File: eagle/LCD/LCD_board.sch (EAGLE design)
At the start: 7 parts, among them CN1 1X4-CLEANBIG

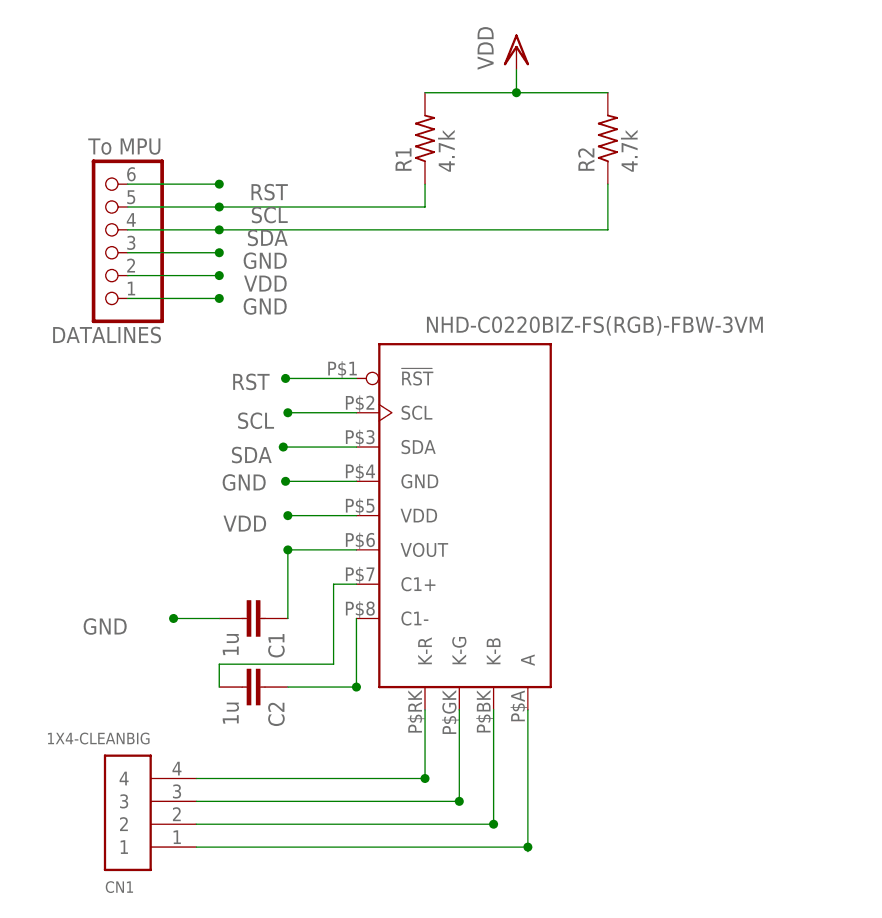
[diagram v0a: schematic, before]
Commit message: Updated LCD_board.sch with modified LCD screen schematic.
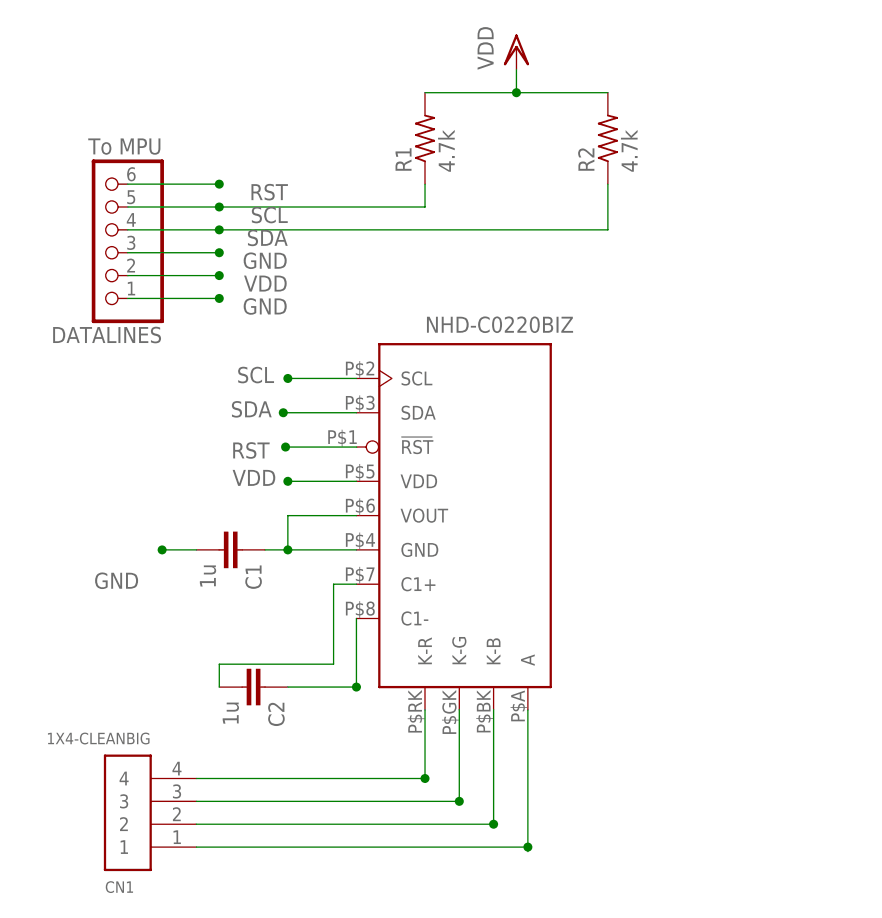
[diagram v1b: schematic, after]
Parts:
- U$1: value NHD-C0220BIZ-FS(RGB)-FBW-3VM -> NHD-C0220BIZ; device LockBox:NHD-C0220BIZ-FS(RGB)-FBW-3VM -> LockBox:NHD-C0220BIZ
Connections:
- net GND: no longer U$1.GND
- net N$3: now also U$1.GND
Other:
- moved on the sheet: C1
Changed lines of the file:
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@@
 <setting verticaltext="up"/>
 </settings>
-<grid distance="0.1" unitdist="inch" unit="inch" style="lines" multiple="1" display="no" altdistance="0.01" altunitdist="inch" altunit="inch"/>
+<grid distance="0.05" unitdist="inch" unit="inch" style="lines" multiple="1" display="yes" altdistance="0.01" altunitdist="inch" altunit="inch"/>
 <layers>
 <layer number="1" name="Top" color="4" fill="1" visible="no" active="no"/>
@@
 </classes>
 <parts>
-<part name="U$1" library="LockBox" deviceset="NHD-C0220BIZ-FS(RGB)-FBW-3VM" device=""/>
 <part name="DATALINES" library="adafruit" deviceset="PINHD-1X6" device="" value="To MPU">
 <attribute name="DATALINES" value=""/>
@@
 <part name="R2" library="LockBox" deviceset="R-US_" device="0204/5" value="4.7k"/>
 <part name="VDD1" library="supply1" deviceset="VDD" device=""/>
+<part name="U$1" library="LockBox" deviceset="NHD-C0220BIZ" device=""/>
 </parts>
 <sheets>
@@
 </plain>
 <instances>
-<instance part="U$1" gate="G$1" x="104.14" y="33.02"/>
 <instance part="DATALINES" gate="A" x="63.5" y="63.5" smashed="yes" rot="R180">
 <attribute name="NAME" x="69.85" y="52.705" size="1.778" layer="95" rot="R180"/>
@@
 <attribute name="DATALINES" x="63.5" y="63.5" size="1.778" layer="96" rot="R180" display="off"/>
 </instance>
-<instance part="C1" gate="G$1" x="81.28" y="20.32" rot="R270"/>
+<instance part="C1" gate="G$1" x="78.74" y="27.94" rot="R270"/>
 <instance part="C2" gate="G$1" x="81.28" y="12.7" rot="R270"/>
 <instance part="CN1" gate="G$1" x="68.58" y="-2.54" rot="R180"/>
@@
 <instance part="R2" gate="G$1" x="119.38" y="73.66" rot="R90"/>
 <instance part="VDD1" gate="G$1" x="109.22" y="83.82"/>
+<instance part="U$1" gate="G$1" x="104.14" y="33.02"/>
 </instances>
 <busses>
@@
 <net name="N$1" class="0">
 <segment>
-<pinref part="U$1" gate="G$1" pin="C1-"/>
 <pinref part="C2" gate="G$1" pin="1"/>
 <wire x1="91.44" y1="20.32" x2="91.44" y2="12.7" width="0.1524" layer="91"/>
 <wire x1="91.44" y1="12.7" x2="83.82" y2="12.7" width="0.1524" layer="91"/>
 <junction x="91.44" y="12.7"/>
+<pinref part="U$1" gate="G$1" pin="C1-"/>
 </segment>
 </net>
@@
 <wire x1="76.2" y1="15.24" x2="88.9" y2="15.24" width="0.1524" layer="91"/>
 <wire x1="88.9" y1="15.24" x2="88.9" y2="24.13" width="0.1524" layer="91"/>
+<wire x1="91.44" y1="24.13" x2="88.9" y2="24.13" width="0.1524" layer="91"/>
 <pinref part="U$1" gate="G$1" pin="C1+"/>
-<wire x1="91.44" y1="24.13" x2="88.9" y2="24.13" width="0.1524" layer="91"/>
 </segment>
 </net>
 <net name="N$3" class="0">
 <segment>
-<pinref part="U$1" gate="G$1" pin="VOUT"/>
 <wire x1="91.44" y1="27.94" x2="83.82" y2="27.94" width="0.1524" layer="91"/>
 <pinref part="C1" gate="G$1" pin="1"/>
-<wire x1="83.82" y1="27.94" x2="83.82" y2="20.32" width="0.1524" layer="91"/>
+<wire x1="83.82" y1="27.94" x2="81.28" y2="27.94" width="0.1524" layer="91"/>
 <junction x="83.82" y="27.94"/>
+<pinref part="U$1" gate="G$1" pin="GND"/>
+<pinref part="U$1" gate="G$1" pin="VOUT"/>
+<wire x1="91.44" y1="31.75" x2="83.82" y2="31.75" width="0.1524" layer="91"/>
+<wire x1="83.82" y1="31.75" x2="83.82" y2="27.94" width="0.1524" layer="91"/>
 </segment>
 </net>
 <net name="RST" class="0">
 <segment>
-<junction x="83.566" y="46.99"/>
-<label x="81.788" y="47.498" size="1.778" layer="95" rot="R180"/>
+<junction x="83.566" y="39.37"/>
+<label x="81.788" y="39.878" size="1.778" layer="95" rot="R180"/>
+<wire x1="91.44" y1="39.37" x2="83.566" y2="39.37" width="0.1524" layer="91"/>
 <pinref part="U$1" gate="G$1" pin="!RST"/>
-<wire x1="91.44" y1="46.99" x2="83.566" y2="46.99" width="0.1524" layer="91"/>
 </segment>
 <segment>
@@
 </segment>
 <segment>
+<wire x1="91.44" y1="46.99" x2="83.82" y2="46.99" width="0.1524" layer="91"/>
+<junction x="83.82" y="46.99"/>
+<label x="82.296" y="48.26" size="1.778" layer="95" rot="R180"/>
 <pinref part="U$1" gate="G$1" pin="SCL"/>
-<wire x1="91.44" y1="43.18" x2="83.82" y2="43.18" width="0.1524" layer="91"/>
-<junction x="83.82" y="43.18"/>
-<label x="82.296" y="43.18" size="1.778" layer="95" rot="R180"/>
 </segment>
 </net>
@@
 </segment>
 <segment>
+<wire x1="91.44" y1="43.18" x2="83.312" y2="43.18" width="0.1524" layer="91"/>
+<junction x="83.312" y="43.18"/>
+<label x="82.042" y="44.45" size="1.778" layer="95" rot="R180"/>
 <pinref part="U$1" gate="G$1" pin="SDA"/>
-<wire x1="91.44" y1="39.37" x2="83.312" y2="39.37" width="0.1524" layer="91"/>
-<junction x="83.312" y="39.37"/>
-<label x="82.042" y="39.37" size="1.778" layer="95" rot="R180"/>
 </segment>
 </net>
@@
 <junction x="76.2" y="58.42"/>
 <label x="83.82" y="58.42" size="1.778" layer="95" rot="R180"/>
-</segment>
-<segment>
-<wire x1="91.44" y1="31.75" x2="83.82" y2="31.75" width="0.1524" layer="91"/>
-<junction x="83.82" y="31.75"/>
-<label x="81.534" y="31.75" size="1.778" layer="95" rot="R180"/>
-<pinref part="U$1" gate="G$1" pin="VDD"/>
 </segment>
 <segment>
@@
 <pinref part="VDD1" gate="G$1" pin="VDD"/>
 </segment>
+<segment>
+<pinref part="U$1" gate="G$1" pin="VDD"/>
+<wire x1="91.44" y1="35.56" x2="83.82" y2="35.56" width="0.1524" layer="91"/>
+<junction x="83.82" y="35.56"/>
+<label x="82.55" y="36.83" size="1.778" layer="95" rot="R180"/>
+</segment>
 </net>
 <net name="GND" class="0">
@@
 </segment>
 <segment>
-<pinref part="U$1" gate="G$1" pin="GND"/>
-<wire x1="91.44" y1="35.56" x2="83.566" y2="35.56" width="0.1524" layer="91"/>
-<junction x="83.566" y="35.56"/>
-<label x="76.454" y="34.544" size="1.778" layer="95"/>
-</segment>
-<segment>
 <pinref part="DATALINES" gate="A" pin="3"/>
 <wire x1="66.04" y1="60.96" x2="76.2" y2="60.96" width="0.1524" layer="91"/>
@@
 <segment>
 <pinref part="C1" gate="G$1" pin="2"/>
-<wire x1="76.2" y1="20.32" x2="71.12" y2="20.32" width="0.1524" layer="91"/>
-<junction x="71.12" y="20.32"/>
-<label x="66.04" y="20.32" size="1.778" layer="95" rot="R180"/>
+<wire x1="73.66" y1="27.94" x2="69.85" y2="27.94" width="0.1524" layer="91"/>
+<junction x="69.85" y="27.94"/>
+<label x="67.31" y="25.4" size="1.778" layer="95" rot="R180"/>
 </segment>
 </net>
 <net name="A" class="0">
 <segment>
-<pinref part="U$1" gate="G$1" pin="K-R"/>
 <pinref part="CN1" gate="G$1" pin="4"/>
 <wire x1="99.06" y1="10.16" x2="99.06" y2="2.54" width="0.1524" layer="91"/>
 <wire x1="99.06" y1="2.54" x2="73.66" y2="2.54" width="0.1524" layer="91"/>
 <junction x="99.06" y="2.54"/>
+<pinref part="U$1" gate="G$1" pin="K-R"/>
 </segment>
 </net>
 <net name="GK" class="0">
 <segment>
-<pinref part="U$1" gate="G$1" pin="K-B"/>
 <wire x1="106.68" y1="10.16" x2="106.68" y2="-2.54" width="0.1524" layer="91"/>
 <pinref part="CN1" gate="G$1" pin="2"/>
 <wire x1="106.68" y1="-2.54" x2="73.66" y2="-2.54" width="0.1524" layer="91"/>
 <junction x="106.68" y="-2.54"/>
+<pinref part="U$1" gate="G$1" pin="K-B"/>
 </segment>
 </net>
 <net name="N$2" class="0">
 <segment>
-<pinref part="U$1" gate="G$1" pin="K-G"/>
 <wire x1="102.87" y1="10.16" x2="102.87" y2="0" width="0.1524" layer="91"/>
 <pinref part="CN1" gate="G$1" pin="3"/>
@@
 <wire x1="102.87" y1="0" x2="73.66" y2="0" width="0.1524" layer="91"/>
 <junction x="102.87" y="0"/>
+<pinref part="U$1" gate="G$1" pin="K-G"/>
 </segment>
 </net>
@@
 <wire x1="110.49" y1="-5.588" x2="110.49" y2="-5.08" width="0.1524" layer="91"/>
 <wire x1="110.49" y1="-5.08" x2="73.66" y2="-5.08" width="0.1524" layer="91"/>
-<pinref part="U$1" gate="G$1" pin="A"/>
 <wire x1="110.49" y1="10.16" x2="110.49" y2="-5.08" width="0.1524" layer="91"/>
 <junction x="110.49" y="-5.08"/>
-</segment>
-</net>
+<pinref part="U$1" gate="G$1" pin="A"/>
+</segment>
+</net>

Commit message: LCD_board.brd is now a one layer board.  Created new Gerber files and updated the GerberFiles/LCD directory with these new files
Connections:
- removed net N$3: C1.1, U$1.GND, U$1.VOUT
- new net N$5: C1.1, U$1.VOUT
- net GND: now also U$1.GND
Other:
- moved on the sheet: C1
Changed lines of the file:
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@@
 <attribute name="DATALINES" x="63.5" y="63.5" size="1.778" layer="96" rot="R180" display="off"/>
 </instance>
-<instance part="C1" gate="G$1" x="78.74" y="27.94" rot="R270"/>
+<instance part="C1" gate="G$1" x="81.28" y="31.75" rot="R270"/>
 <instance part="C2" gate="G$1" x="81.28" y="12.7" rot="R270"/>
 <instance part="CN1" gate="G$1" x="68.58" y="-2.54" rot="R180"/>
@@
 <wire x1="91.44" y1="24.13" x2="88.9" y2="24.13" width="0.1524" layer="91"/>
 <pinref part="U$1" gate="G$1" pin="C1+"/>
-</segment>
-</net>
-<net name="N$3" class="0">
-<segment>
-<wire x1="91.44" y1="27.94" x2="83.82" y2="27.94" width="0.1524" layer="91"/>
-<pinref part="C1" gate="G$1" pin="1"/>
-<wire x1="83.82" y1="27.94" x2="81.28" y2="27.94" width="0.1524" layer="91"/>
-<junction x="83.82" y="27.94"/>
-<pinref part="U$1" gate="G$1" pin="GND"/>
-<pinref part="U$1" gate="G$1" pin="VOUT"/>
-<wire x1="91.44" y1="31.75" x2="83.82" y2="31.75" width="0.1524" layer="91"/>
-<wire x1="83.82" y1="31.75" x2="83.82" y2="27.94" width="0.1524" layer="91"/>
 </segment>
 </net>
@@
 <segment>
 <pinref part="C1" gate="G$1" pin="2"/>
+<wire x1="76.2" y1="31.75" x2="73.66" y2="31.75" width="0.1524" layer="91"/>
+<wire x1="73.66" y1="31.75" x2="73.66" y2="27.94" width="0.1524" layer="91"/>
+<wire x1="73.66" y1="27.94" x2="91.44" y2="27.94" width="0.1524" layer="91"/>
 <wire x1="73.66" y1="27.94" x2="69.85" y2="27.94" width="0.1524" layer="91"/>
 <junction x="69.85" y="27.94"/>
 <label x="67.31" y="25.4" size="1.778" layer="95" rot="R180"/>
+<pinref part="U$1" gate="G$1" pin="GND"/>
+<junction x="73.66" y="27.94"/>
 </segment>
 </net>
@@
 </segment>
 </net>
+<net name="N$5" class="0">
+<segment>
+<pinref part="U$1" gate="G$1" pin="VOUT"/>
+<wire x1="91.44" y1="31.75" x2="83.82" y2="31.75" width="0.1524" layer="91"/>
+<pinref part="C1" gate="G$1" pin="1"/>
+</segment>
+</net>
